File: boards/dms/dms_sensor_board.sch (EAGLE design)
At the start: 24 parts, among them Q1 IRLML5203

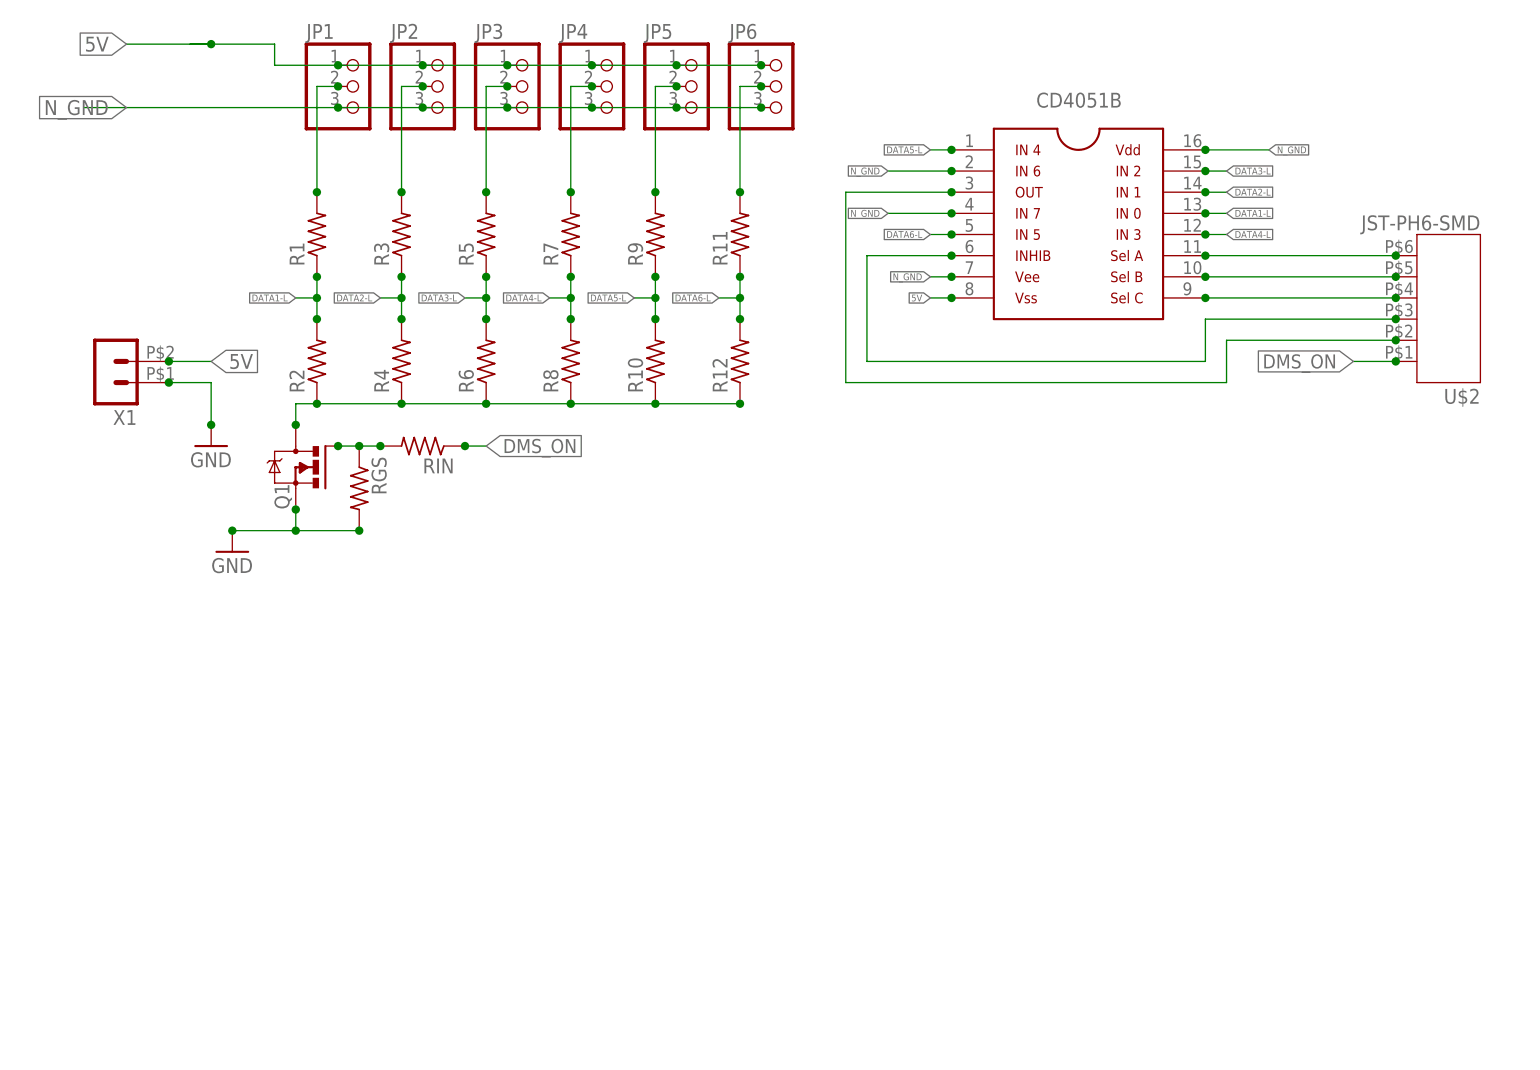
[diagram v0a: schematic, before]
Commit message: Changing boards for fet and text improvements
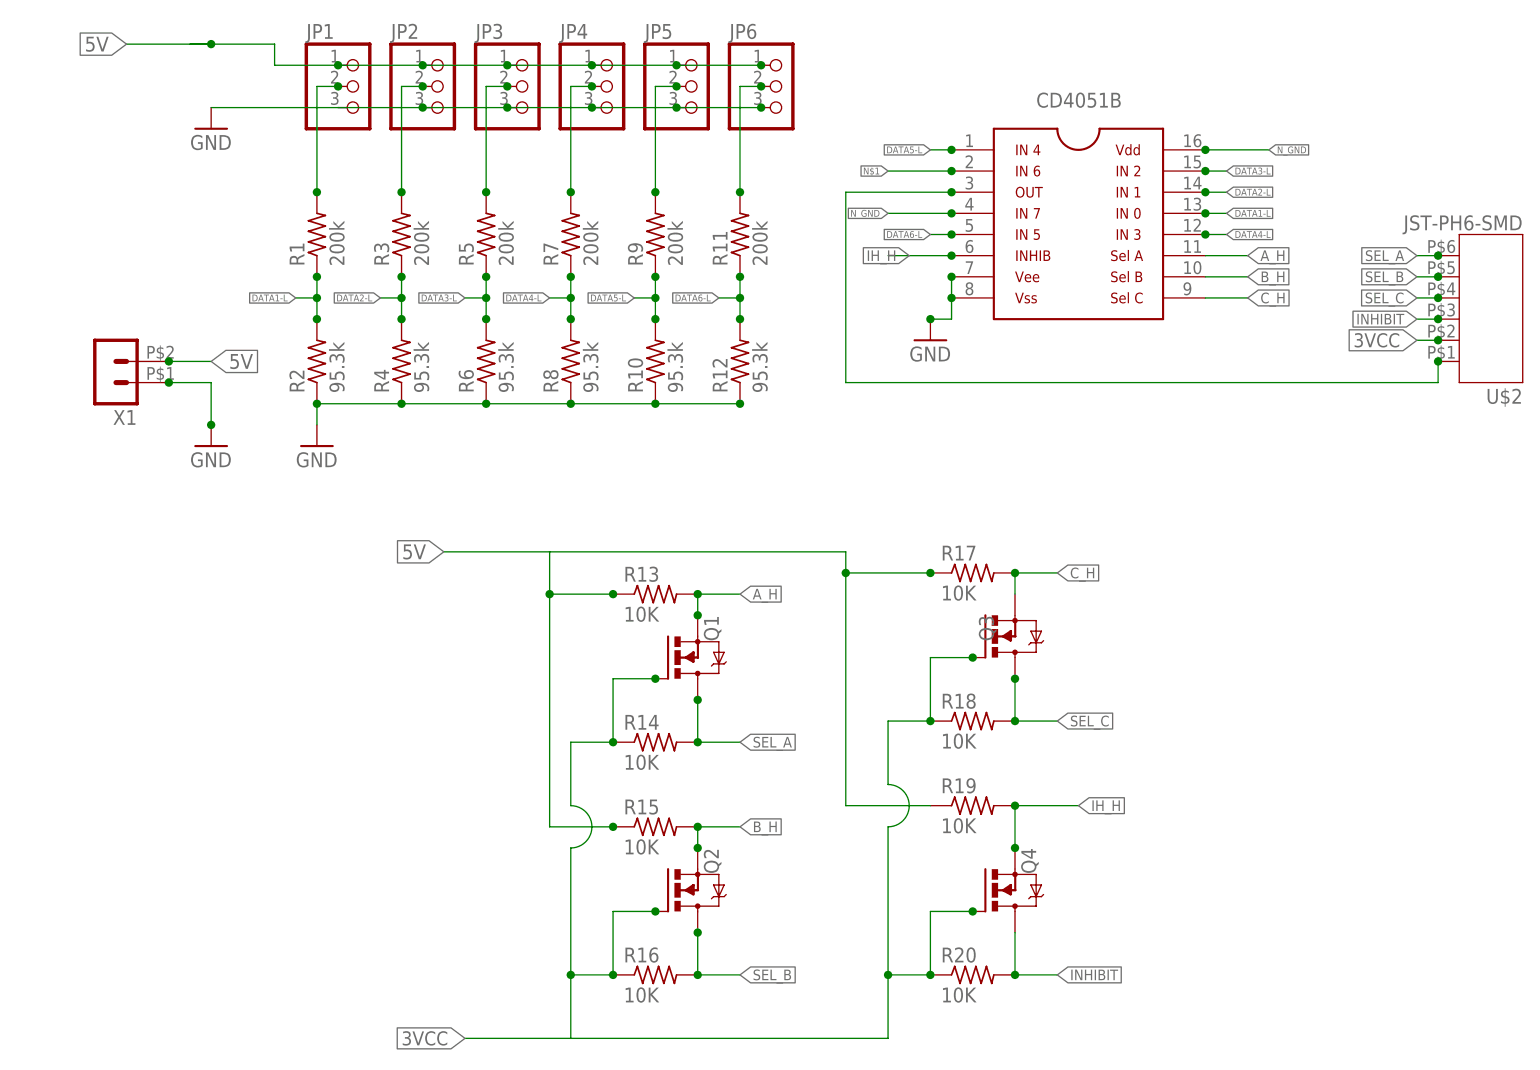
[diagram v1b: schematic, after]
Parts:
- removed RGS, RIN: (no value), resistor:R-US_R0805
- added Q2, Q3, Q4: IRLML5203, ngohara_parts:IRLML5203
- added R13, R14, R15, R16, R17, R18, R19, R20: 10K, resistor:R-US_R0805
- R1, R11, R3, R5, R7, R9: value (none) -> 200k
- R10, R12, R2, R4, R6, R8: value (none) -> 95.3k
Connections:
- removed net DMS_ON: RIN.1, U$2.1
- removed net N$2: MUX1.P$10, U$2.5
- removed net N$3: MUX1.P$9, U$2.4
- removed net N$4: MUX1.P$6, U$2.3
- removed net N$8: Q1.G, RGS.1, RIN.2
- new net 3VCC: Q1.G, Q2.G, Q3.G, Q4.G, R14.1, R16.1, R18.1, R20.1, U$2.2
- new net A_H: Q1.S, R13.2
- new net B_H: Q2.S, R15.2
- new net C_H: Q3.S, R17.2
- new net IH_H: MUX1.P$6, Q4.S, R19.2
- new net INHIBIT: Q4.D, R20.2, U$2.3
- new net SEL_A: Q1.D, R14.2, U$2.6
- new net SEL_B: Q2.D, R16.2, U$2.5
- new net SEL_C: Q3.D, R18.2, U$2.4
- net 5V: now also R13.1, R15.1, R17.1, R19.1; no longer MUX1.P$8
- net GND: now also JP1.3, JP2.3, JP3.3, JP4.3, JP5.3, JP6.3, MUX1.P$7, MUX1.P$8, R10.1, R12.1, R2.1, R4.1, R6.1, R8.1; no longer Q1.S, RGS.2
- net N$1: now also MUX1.P$2; no longer MUX1.P$11, U$2.6
- net N$5: now also U$2.1; no longer U$2.2
- net N_GND: no longer JP1.3, JP2.3, JP3.3, JP4.3, JP5.3, JP6.3, MUX1.P$2, MUX1.P$7, Q1.D, R10.1, R12.1, R2.1, R4.1, R6.1, R8.1
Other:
- moved on the sheet: Q1, U$2

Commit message: changes for new boards, cleared DRC
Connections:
- removed net N$1: MUX1.P$2
- removed net N_GND: MUX1.P$16, MUX1.P$4
- net 5V: now also MUX1.P$16
- net A_H: now also MUX1.P$11
- net B_H: now also MUX1.P$10
- net C_H: now also MUX1.P$9
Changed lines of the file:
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@@
 </variantdefs>
 <classes>
-<class number="0" name="default" width="0.254" drill="0.508">
+<class number="0" name="default" width="0.381" drill="0.508">
 <clearance class="0" value="0.254"/>
 </class>
-<class number="1" name="power" width="0.508" drill="0.508">
+<class number="1" name="power" width="0.635" drill="0.508">
 <clearance class="1" value="0.508"/>
 </class>
@@
 <junction x="15.24" y="55.88"/>
 <wire x1="15.24" y1="55.88" x2="12.7" y2="55.88" width="0.1524" layer="91"/>
+<wire x1="144.78" y1="43.18" x2="134.62" y2="43.18" width="0.1524" layer="91"/>
+<label x="144.78" y="43.18" size="1.27" layer="95" xref="yes"/>
+<pinref part="MUX1" gate="G$1" pin="P$16"/>
+<junction x="134.62" y="43.18"/>
 </segment>
 <segment>
@@
 </segment>
 </net>
-<net name="N_GND" class="1">
-<segment>
-<pinref part="MUX1" gate="G$1" pin="P$4"/>
-<junction x="104.14" y="35.56"/>
-<wire x1="96.52" y1="35.56" x2="104.14" y2="35.56" width="0.1524" layer="91"/>
-<label x="96.52" y="35.56" size="0.8128" layer="95" ratio="12" rot="R180" xref="yes"/>
-</segment>
-<segment>
-<wire x1="142.24" y1="43.18" x2="134.62" y2="43.18" width="0.1524" layer="91"/>
-<pinref part="MUX1" gate="G$1" pin="P$16"/>
-<junction x="134.62" y="43.18"/>
-<label x="142.24" y="43.18" size="0.8128" layer="95" ratio="12" xref="yes"/>
-</segment>
-</net>
 <net name="A_H" class="0">
 <segment>
@@
 <label x="139.7" y="30.48" size="1.27" layer="95" xref="yes"/>
 <junction x="73.66" y="-12.7"/>
+<pinref part="MUX1" gate="G$1" pin="P$11"/>
+<junction x="134.62" y="30.48"/>
 </segment>
 </net>
@@
 <label x="139.7" y="27.94" size="1.27" layer="95" xref="yes"/>
 <junction x="73.66" y="-40.64"/>
+<pinref part="MUX1" gate="G$1" pin="P$10"/>
+<junction x="134.62" y="27.94"/>
 </segment>
 </net>
@@
 <wire x1="134.62" y1="25.4" x2="139.7" y2="25.4" width="0.1524" layer="91"/>
 <label x="139.7" y="25.4" size="1.27" layer="95" xref="yes"/>
+<pinref part="MUX1" gate="G$1" pin="P$9"/>
+<junction x="134.62" y="25.4"/>
 </segment>
 </net>
@@
 </segment>
 </net>
-<net name="N$1" class="1">
-<segment>
-<pinref part="MUX1" gate="G$1" pin="P$2"/>
-<junction x="104.14" y="40.64"/>
-<wire x1="96.52" y1="40.64" x2="104.14" y2="40.64" width="0.1524" layer="91"/>
-<label x="96.52" y="40.64" size="0.8128" layer="95" ratio="12" rot="R180" xref="yes"/>
-</segment>
-</net>

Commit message: Fixed Mux padsize, cleared relavent DRC errors
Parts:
- removed MUX1: 8X1, ngohara_parts:8X1_ANALOG_MUX
- added U$1: MUX16BANALOG, wolfbot_specific_parts:MUX16BANALOG
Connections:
- net 5V: now also U$1.VDD; no longer MUX1.P$16
- net A_H: now also U$1.SELA; no longer MUX1.P$11
- net B_H: now also U$1.SELB; no longer MUX1.P$10
- net C_H: now also U$1.SELC; no longer MUX1.P$9
- net DATA1-L: now also U$1.IN0; no longer MUX1.P$13
- net DATA2-L: now also U$1.IN1; no longer MUX1.P$14
- net DATA3-L: now also U$1.IN2; no longer MUX1.P$15
- net DATA4-L: now also U$1.IN3; no longer MUX1.P$12
- net DATA5-L: now also U$1.IN4; no longer MUX1.P$1
- net DATA6-L: now also U$1.IN5; no longer MUX1.P$5
- net GND: now also U$1.VEE, U$1.VSS; no longer MUX1.P$7, MUX1.P$8
- net IH_H: now also U$1.INHIB; no longer MUX1.P$6
- net N$5: now also U$1.OUT; no longer MUX1.P$3
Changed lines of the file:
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@@
 <?xml version="1.0" encoding="utf-8"?>
 <!DOCTYPE eagle SYSTEM "eagle.dtd">
-<eagle version="6.4">
+<eagle version="6.5.0">
 <drawing>
 <settings>
@@
 <part name="GND1" library="supply1" deviceset="GND" device=""/>
 <part name="Q1" library="ngohara_parts" deviceset="IRLML5203" device=""/>
-<part name="MUX1" library="ngohara_parts" deviceset="8X1_ANALOG_MUX" device="" value="8X1"/>
 <part name="GND3" library="supply1" deviceset="GND" device=""/>
 <part name="R13" library="resistor" deviceset="R-US_" device="R0805" value="10K"/>
@@
 <part name="GND2" library="supply1" deviceset="GND" device=""/>
 <part name="GND4" library="supply1" deviceset="GND" device=""/>
+<part name="U$1" library="wolfbot_specific_parts" deviceset="MUX16BANALOG" device=""/>
 </parts>
 <sheets>
@@
 <attribute name="NAME" x="76.2" y="-12.7" size="1.778" layer="95" rot="MR270"/>
 </instance>
-<instance part="MUX1" gate="G$1" x="119.38" y="33.02"/>
 <instance part="GND3" gate="1" x="27.94" y="7.62"/>
 <instance part="R13" gate="G$1" x="68.58" y="-10.16"/>
@@
 <instance part="GND2" gate="1" x="101.6" y="20.32"/>
 <instance part="GND4" gate="1" x="15.24" y="45.72"/>
+<instance part="U$1" gate="G$1" x="119.38" y="33.02"/>
 </instances>
 <busses>
@@
 </segment>
 <segment>
-<pinref part="MUX1" gate="G$1" pin="P$7"/>
 <pinref part="GND2" gate="1" pin="GND"/>
 <wire x1="104.14" y1="27.94" x2="104.14" y2="25.4" width="0.1524" layer="91"/>
@@
 <wire x1="104.14" y1="22.86" x2="101.6" y2="22.86" width="0.1524" layer="91"/>
 <junction x="101.6" y="22.86"/>
-<pinref part="MUX1" gate="G$1" pin="P$8"/>
+<pinref part="U$1" gate="G$1" pin="VEE"/>
+<pinref part="U$1" gate="G$1" pin="VSS"/>
 <junction x="104.14" y="25.4"/>
 <junction x="104.14" y="27.94"/>
@@
 <wire x1="144.78" y1="43.18" x2="134.62" y2="43.18" width="0.1524" layer="91"/>
 <label x="144.78" y="43.18" size="1.27" layer="95" xref="yes"/>
-<pinref part="MUX1" gate="G$1" pin="P$16"/>
+<pinref part="U$1" gate="G$1" pin="VDD"/>
 <junction x="134.62" y="43.18"/>
 </segment>
@@
 <wire x1="134.62" y1="35.56" x2="137.16" y2="35.56" width="0.1524" layer="91"/>
 <label x="137.16" y="35.56" size="0.8128" layer="95" ratio="12" xref="yes"/>
-<pinref part="MUX1" gate="G$1" pin="P$13"/>
+<pinref part="U$1" gate="G$1" pin="IN0"/>
 <junction x="134.62" y="35.56"/>
 </segment>
@@
 <wire x1="134.62" y1="38.1" x2="137.16" y2="38.1" width="0.1524" layer="91"/>
 <label x="137.16" y="38.1" size="0.8128" layer="95" ratio="12" xref="yes"/>
-<pinref part="MUX1" gate="G$1" pin="P$14"/>
+<pinref part="U$1" gate="G$1" pin="IN1"/>
 <junction x="134.62" y="38.1"/>
 </segment>
@@
 <wire x1="134.62" y1="40.64" x2="137.16" y2="40.64" width="0.1524" layer="91"/>
 <label x="137.16" y="40.64" size="0.8128" layer="95" ratio="12" xref="yes"/>
-<pinref part="MUX1" gate="G$1" pin="P$15"/>
+<pinref part="U$1" gate="G$1" pin="IN2"/>
 <junction x="134.62" y="40.64"/>
 </segment>
@@
 <wire x1="134.62" y1="33.02" x2="137.16" y2="33.02" width="0.1524" layer="91"/>
 <label x="137.16" y="33.02" size="0.8128" layer="95" ratio="12" xref="yes"/>
-<pinref part="MUX1" gate="G$1" pin="P$12"/>
+<pinref part="U$1" gate="G$1" pin="IN3"/>
 <junction x="134.62" y="33.02"/>
 </segment>
@@
 <wire x1="104.14" y1="43.18" x2="101.6" y2="43.18" width="0.1524" layer="91"/>
 <label x="101.6" y="43.18" size="0.8128" layer="95" ratio="12" rot="R180" xref="yes"/>
-<pinref part="MUX1" gate="G$1" pin="P$1"/>
+<pinref part="U$1" gate="G$1" pin="IN4"/>
 <junction x="104.14" y="43.18"/>
 </segment>
@@
 <wire x1="104.14" y1="33.02" x2="101.6" y2="33.02" width="0.1524" layer="91"/>
 <label x="101.6" y="33.02" size="0.8128" layer="95" ratio="12" rot="R180" xref="yes"/>
-<pinref part="MUX1" gate="G$1" pin="P$5"/>
+<pinref part="U$1" gate="G$1" pin="IN5"/>
 <junction x="104.14" y="33.02"/>
 </segment>
@@
 <wire x1="91.44" y1="15.24" x2="162.56" y2="15.24" width="0.1524" layer="91"/>
 <wire x1="162.56" y1="15.24" x2="162.56" y2="17.78" width="0.1524" layer="91"/>
-<pinref part="MUX1" gate="G$1" pin="P$3"/>
-<junction x="104.14" y="38.1"/>
 <pinref part="U$2" gate="G$1" pin="1"/>
 <junction x="162.56" y="17.78"/>
+<pinref part="U$1" gate="G$1" pin="OUT"/>
+<junction x="104.14" y="38.1"/>
 </segment>
 </net>
@@
 <label x="139.7" y="30.48" size="1.27" layer="95" xref="yes"/>
 <junction x="73.66" y="-12.7"/>
-<pinref part="MUX1" gate="G$1" pin="P$11"/>
+<pinref part="U$1" gate="G$1" pin="SELA"/>
 <junction x="134.62" y="30.48"/>
 </segment>
@@
 <label x="139.7" y="27.94" size="1.27" layer="95" xref="yes"/>
 <junction x="73.66" y="-40.64"/>
-<pinref part="MUX1" gate="G$1" pin="P$10"/>
+<pinref part="U$1" gate="G$1" pin="SELB"/>
 <junction x="134.62" y="27.94"/>
 </segment>
@@
 <wire x1="134.62" y1="25.4" x2="139.7" y2="25.4" width="0.1524" layer="91"/>
 <label x="139.7" y="25.4" size="1.27" layer="95" xref="yes"/>
-<pinref part="MUX1" gate="G$1" pin="P$9"/>
+<pinref part="U$1" gate="G$1" pin="SELC"/>
 <junction x="134.62" y="25.4"/>
 </segment>
@@
 <label x="119.38" y="-35.56" size="1.27" layer="95" xref="yes"/>
 <wire x1="96.52" y1="30.48" x2="104.14" y2="30.48" width="0.1524" layer="91"/>
-<pinref part="MUX1" gate="G$1" pin="P$6"/>
-<junction x="104.14" y="30.48"/>
 <label x="99.06" y="30.48" size="1.27" layer="95" rot="R180" xref="yes"/>
 <junction x="111.76" y="-40.64"/>
-</segment>
-</net>
+<pinref part="U$1" gate="G$1" pin="INHIB"/>
+<junction x="104.14" y="30.48"/>
+</segment>
+</net>
